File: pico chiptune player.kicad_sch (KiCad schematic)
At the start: 40 parts, among them J2 MicroSD, J3 Speaker_L, J4 Speaker_R, SW1 Play / Pause, SW2 Next, SW3 Previous, U1 YM2149F, U2 0.96"OLED_I2C, U3 PAM8403, U4 YM2149F

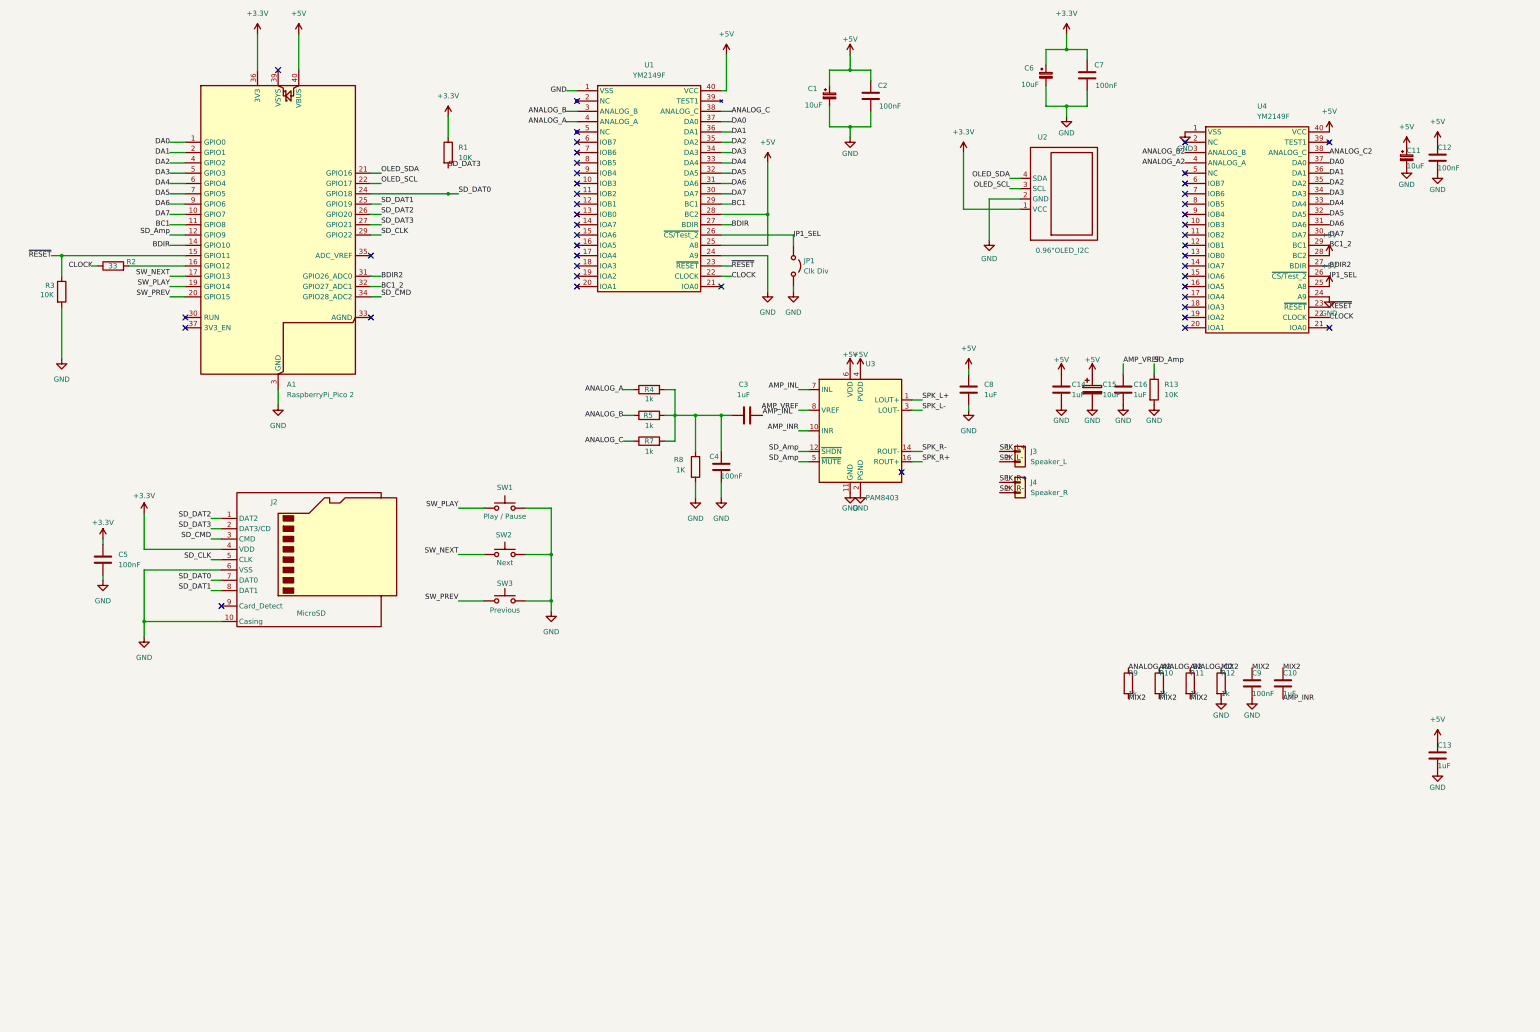
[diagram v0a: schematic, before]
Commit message: feat(hw): upgrade to Rev 0.7 with bare RP2354A, USB-C 3-stage sequencer, and 4-mode 74HCT4053D stereo/mono mixing matrix
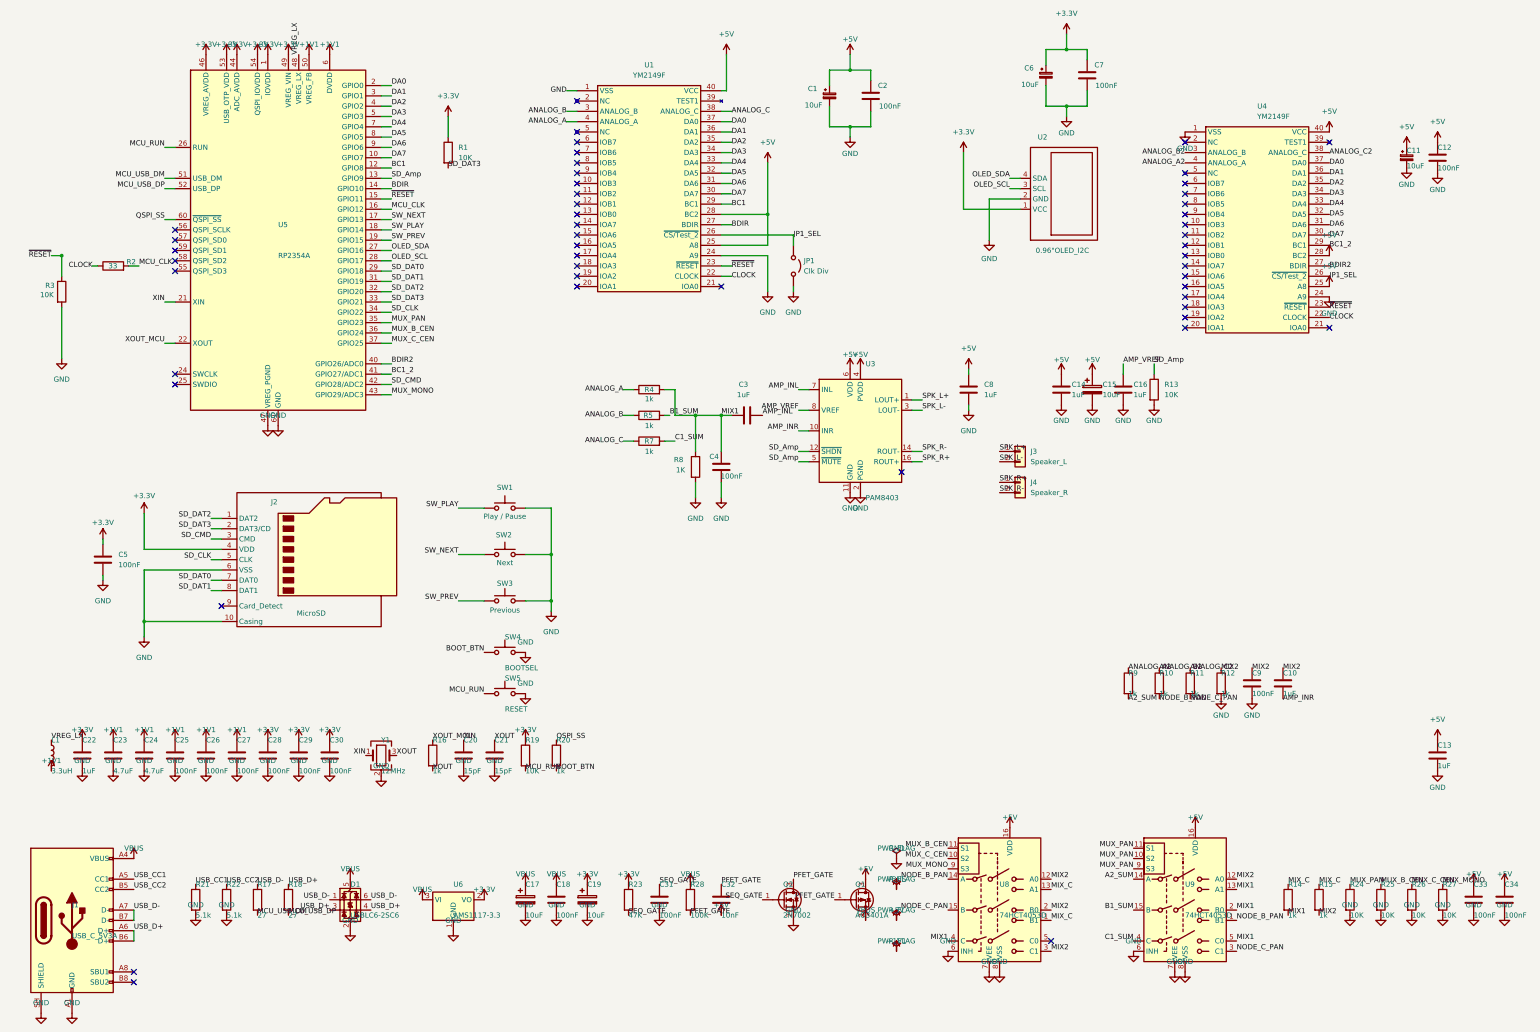
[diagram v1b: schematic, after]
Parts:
- removed A1: RaspberryPi_Pico 2, TMCu Module:RPi_Pico_SMD_TH, symbol MCU_Module_RaspberryPi_Pico:RaspberryPi_Pico
- added C17, C19: 10uF, Capacitor_SMD:CP_Elec_4x5.4, symbol Device:C_Polarized
- added C18, C25, C26, C27, C28, C29, C30, C31, C33, C34: 100nF, Capacitor_SMD:C_0805_2012Metric_Pad1.18x1.45mm_HandSolder, symbol Device:C
- added C20, C21: 15pF, Capacitor_SMD:C_0805_2012Metric_Pad1.18x1.45mm_HandSolder, symbol Device:C
- added C22: 1uF, Capacitor_SMD:C_0805_2012Metric_Pad1.18x1.45mm_HandSolder, symbol Device:C
- added C23, C24: 4.7uF, Capacitor_SMD:C_0805_2012Metric_Pad1.18x1.45mm_HandSolder, symbol Device:C
- added C32: 10nF, Capacitor_SMD:C_0805_2012Metric_Pad1.18x1.45mm_HandSolder, symbol Device:C
- added D1: USBLC6-2SC6, Package_TO_SOT_SMD:SOT-23-6, symbol Power_Protection:USBLC6-2SC6
- added J1: USB_C_5V3A, Connector_USB:USB_C_Receptacle_HRO_TYPE-C-31-M-12, symbol Connector:USB_C_Receptacle_USB2.0_16P
- added L1: 3.3uH, Inductor_SMD:L_1210_3225Metric, symbol Device:L
- added Q1: AO3401A, Package_TO_SOT_SMD:SOT-23, symbol Transistor_FET:AO3401A
- added Q2: 2N7002, Package_TO_SOT_SMD:SOT-23, symbol Transistor_FET:2N7002
- added R14, R15, R16, R20: 1k, Resistor_SMD:R_0805_2012Metric_Pad1.20x1.40mm_HandSolder, symbol Device:R
- added R17, R18: 27, Resistor_SMD:R_0805_2012Metric_Pad1.20x1.40mm_HandSolder, symbol Device:R
- added R19, R24, R25, R26, R27: 10K, Resistor_SMD:R_0805_2012Metric_Pad1.20x1.40mm_HandSolder, symbol Device:R
- added R21, R22: 5.1k, Resistor_SMD:R_0805_2012Metric_Pad1.20x1.40mm_HandSolder, symbol Device:R
- added R23: 47K, Resistor_SMD:R_0805_2012Metric_Pad1.20x1.40mm_HandSolder, symbol Device:R
- added R28: 100K, Resistor_SMD:R_0805_2012Metric_Pad1.20x1.40mm_HandSolder, symbol Device:R
- added SW4: BOOTSEL, Button_Switch_THT:SW_PUSH_6mm, symbol Switch:SW_Push
- added SW5: RESET, Button_Switch_THT:SW_PUSH_6mm, symbol Switch:SW_Push
- added U5: RP2354A, Package_DFN_QFN:QFN-60-1EP_7x7mm_P0.4mm_EP3.4x3.4mm, symbol MCU_RaspberryPi:RP2354A
- added U6: AMS1117-3.3, Package_TO_SOT_SMD:SOT-223-3_TabPin2, symbol Regulator_Linear:AMS1117-3.3
- added U8, U9: 74HCT4053D, Package_SO:SOIC-16_3.9x9.9mm_P1.27mm, symbol Analog_Switch:CD4053B
- added Y1: 12MHz, Crystal:Crystal_SMD_3225-4Pin_3.2x2.5mm, symbol Device:Crystal_GND24
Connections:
- net +3.3V: now also C19.1, C22.1, C28.1, C29.1, C30.1, R19.1, R23.1, U5.1 (IOVDD), U5.11 (IOVDD), U5.20 (IOVDD), U5.30 (IOVDD), U5.38 (IOVDD), U5.44 (ADC_AVDD), U5.45 (IOVDD), U5.46 (VREG_AVDD), U5.49 (VREG_VIN), U5.53 (USB_OTP_VDD), U5.54 (QSPI_IOVDD), U6.2 (VO)
- net +5V: now also C32.2, C33.1, C34.1, Q1.3 (D), U8.16 (VDD), U9.16 (VDD)
- net BC1: now also U5.12 (GPIO8)
- net BC1_2: now also U5.41 (GPIO27/ADC1)
- net BDIR: now also U5.14 (GPIO10)
- net BDIR2: now also U5.40 (GPIO26/ADC0)
- net DA0: now also U5.2 (GPIO0)
- net DA1: now also U5.3 (GPIO1)
- net DA2: now also U5.4 (GPIO2)
- net DA3: now also U5.5 (GPIO3)
- net DA4: now also U5.7 (GPIO4)
- net DA5: now also U5.8 (GPIO5)
- net DA6: now also U5.9 (GPIO6)
- net DA7: now also U5.10 (GPIO7)
- net GND: now also C17.2, C18.2, C19.2, C20.2, C21.2, C22.2, C23.2, C24.2, C25.2, C26.2, C27.2, C28.2, C29.2, C30.2, C31.2, C33.2, C34.2, D1.2 (GND), J1.A1 (GND), J1.A12 (GND), J1.B1 (GND), J1.B12 (GND), J1.SH (SHIELD), Q2.2 (S), R21.2, R22.2, R24.2, R25.2, R26.2, R27.2, SW4.2, SW5.2, U5.47 (VREG_PGND), U5.61 (GND), U6.1 (GND), U8.6 (INH), U8.7 (VEE), U8.8 (VSS), U9.6 (INH), U9.7 (VEE), U9.8 (VSS), Y1.2 (G), Y1.4 (G)
- net MIX2: now also R15.2, U8.12 (A0), U8.2 (B0), U8.3 (C1), U9.12 (A0); no longer R10.2, R11.2, R9.2
- net OLED_SCL: now also U5.28 (GPIO17)
- net OLED_SDA: now also U5.27 (GPIO16)
- net SD_Amp: now also U5.13 (GPIO9)
- net SD_CLK: now also U5.34 (GPIO22)
- net SD_CMD: now also U5.42 (GPIO28/ADC2)
- net SD_DAT0: now also U5.29 (GPIO18)
- net SD_DAT1: now also U5.31 (GPIO19)
- net SD_DAT2: now also U5.32 (GPIO20)
- net SD_DAT3: now also U5.33 (GPIO21)
- net SW_NEXT: now also U5.17 (GPIO13)
- net SW_PLAY: now also U5.18 (GPIO14)
- net SW_PREV: now also U5.19 (GPIO15)
- net ~{RESET}: now also U5.15 (GPIO11)
- net MIX1: now reaches C3.1, C4.1, R4.2, R8.1
- net MIX1: now also R14.2, U8.4 (C), U9.13 (A1), U9.2 (B0), U9.5 (C0); no longer R5.2, R7.2
- net MCU_CLK: now reaches R2.2
- net MCU_CLK: now also U5.16 (GPIO12)
- new net +1V1: C23.1, C24.1, C25.1, C26.1, C27.1, L1.2, U5.23 (DVDD), U5.39 (DVDD), U5.50 (VREG_FB), U5.6 (DVDD)
- new net A2_SUM: R9.2, U9.14 (A)
- new net B1_SUM: R5.2, U9.15 (B)
- new net BOOT_BTN: R20.2, SW4.1
- new net C1_SUM: R7.2, U9.4 (C)
- new net MCU_RUN: R19.2, SW5.1, U5.26 (RUN)
- new net MCU_USB_DM: R17.2, U5.51 (USB_DM)
- new net MCU_USB_DP: R18.2, U5.52 (USB_DP)
- new net MIX_C: R14.1, R15.1, U8.1 (B1), U8.13 (A1)
- new net MUX_B_CEN: R25.1, U5.36 (GPIO24), U8.11 (S1)
- new net MUX_C_CEN: R26.1, U5.37 (GPIO25), U8.10 (S2)
- new net MUX_MONO: R27.1, U5.43 (GPIO29/ADC3), U8.9 (S3)
- new net MUX_PAN: R24.1, U5.35 (GPIO23), U9.10 (S2), U9.11 (S1), U9.9 (S3)
- new net NODE_B_PAN: R10.2, U8.14 (A), U9.1 (B1)
- new net NODE_C_PAN: R11.2, U8.15 (B), U9.3 (C1)
- new net PFET_GATE: C32.1, Q1.1 (G), Q2.3 (D), R28.2
- new net QSPI_SS: R20.1, U5.60 (~{QSPI_SS})
- new net SEQ_GATE: C31.1, Q2.1 (G), R23.2
- new net USB_CC1: J1.A5 (CC1), R21.1
- new net USB_CC2: J1.B5 (CC2), R22.1
- new net USB_D+: D1.3 (I/O2), D1.4 (I/O2), J1.A6 (D+), J1.B6 (D+), R18.1
- new net USB_D-: D1.1 (I/O1), D1.6 (I/O1), J1.A7 (D-), J1.B7 (D-), R17.1
- new net VBUS: C17.1, C18.1, D1.5 (VBUS), J1.A4 (VBUS), J1.A9 (VBUS), J1.B4 (VBUS), J1.B9 (VBUS), Q1.2 (S), R28.1, U6.3 (VI)
- new net VREG_LX: L1.1, U5.48 (VREG_LX)
- new net XIN: C20.1, U5.21 (XIN), Y1.1
- new net XOUT: C21.1, R16.2, Y1.3
- new net XOUT_MCU: R16.1, U5.22 (XOUT)
- no-connect marks 44 -> 49

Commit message: Implement code changes to enhance functionality and improve performance
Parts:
- removed C17, C19: 10uF, Capacitor_SMD:CP_Elec_4x5.4, symbol Device:C_Polarized
- removed C18, C25, C26, C27, C28, C29, C30, C31, C33, C34: 100nF, Capacitor_SMD:C_0805_2012Metric_Pad1.18x1.45mm_HandSolder, symbol Device:C
- removed C20, C21: 15pF, Capacitor_SMD:C_0805_2012Metric_Pad1.18x1.45mm_HandSolder, symbol Device:C
- removed C22: 1uF, Capacitor_SMD:C_0805_2012Metric_Pad1.18x1.45mm_HandSolder, symbol Device:C
- removed C23, C24: 4.7uF, Capacitor_SMD:C_0805_2012Metric_Pad1.18x1.45mm_HandSolder, symbol Device:C
- removed C32: 10nF, Capacitor_SMD:C_0805_2012Metric_Pad1.18x1.45mm_HandSolder, symbol Device:C
- removed D1: USBLC6-2SC6, Package_TO_SOT_SMD:SOT-23-6, symbol Power_Protection:USBLC6-2SC6
- removed J1: USB_C_5V3A, Connector_USB:USB_C_Receptacle_HRO_TYPE-C-31-M-12, symbol Connector:USB_C_Receptacle_USB2.0_16P
- removed L1: 3.3uH, Inductor_SMD:L_1210_3225Metric, symbol Device:L
- removed Q1: AO3401A, Package_TO_SOT_SMD:SOT-23, symbol Transistor_FET:AO3401A
- removed Q2: 2N7002, Package_TO_SOT_SMD:SOT-23, symbol Transistor_FET:2N7002
- removed R14, R15, R16, R20: 1k, Resistor_SMD:R_0805_2012Metric_Pad1.20x1.40mm_HandSolder, symbol Device:R
- removed R17, R18: 27, Resistor_SMD:R_0805_2012Metric_Pad1.20x1.40mm_HandSolder, symbol Device:R
- removed R19, R24, R25, R26, R27: 10K, Resistor_SMD:R_0805_2012Metric_Pad1.20x1.40mm_HandSolder, symbol Device:R
- removed R21, R22: 5.1k, Resistor_SMD:R_0805_2012Metric_Pad1.20x1.40mm_HandSolder, symbol Device:R
- removed R23: 47K, Resistor_SMD:R_0805_2012Metric_Pad1.20x1.40mm_HandSolder, symbol Device:R
- removed R28: 100K, Resistor_SMD:R_0805_2012Metric_Pad1.20x1.40mm_HandSolder, symbol Device:R
- removed SW4: BOOTSEL, Button_Switch_THT:SW_PUSH_6mm, symbol Switch:SW_Push
- removed SW5: RESET, Button_Switch_THT:SW_PUSH_6mm, symbol Switch:SW_Push
- removed U5: RP2354A, Package_DFN_QFN:QFN-60-1EP_7x7mm_P0.4mm_EP3.4x3.4mm, symbol MCU_RaspberryPi:RP2354A
- removed U6: AMS1117-3.3, Package_TO_SOT_SMD:SOT-223-3_TabPin2, symbol Regulator_Linear:AMS1117-3.3
- removed U8, U9: 74HCT4053D, Package_SO:SOIC-16_3.9x9.9mm_P1.27mm, symbol Analog_Switch:CD4053B
- removed Y1: 12MHz, Crystal:Crystal_SMD_3225-4Pin_3.2x2.5mm, symbol Device:Crystal_GND24
- added A1: RaspberryPi_Pico 2, TMCu Module:RPi_Pico_SMD_TH, symbol MCU_Module_RaspberryPi_Pico:RaspberryPi_Pico
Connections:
- net A2_SUM is gone; now on net MIX2: R9.2
- net C1_SUM is gone; now on an unnamed net: R7.2
- net MIX1 is gone; now on an unnamed net: C3.1, C4.1, R4.2, R8.1
- net NODE_B_PAN is gone; now on net MIX2: R10.2
- net NODE_C_PAN is gone; now on net MIX2: R11.2
- net +3.3V: now also A1.36 (3V3)
- net +5V: now also A1.40 (VBUS)
- net BC1: now also A1.11 (GPIO8)
- net BC1_2: now also A1.32 (GPIO27_ADC1)
- net BDIR: now also A1.14 (GPIO10)
- net BDIR2: now also A1.31 (GPIO26_ADC0)
- net DA0: now also A1.1 (GPIO0)
- net DA1: now also A1.2 (GPIO1)
- net DA2: now also A1.4 (GPIO2)
- net DA3: now also A1.5 (GPIO3)
- net DA4: now also A1.6 (GPIO4)
- net DA5: now also A1.7 (GPIO5)
- net DA6: now also A1.9 (GPIO6)
- net DA7: now also A1.10 (GPIO7)
- net GND: now also A1.13 (GND), A1.18 (GND), A1.23 (GND), A1.28 (GND), A1.3 (GND), A1.38 (GND), A1.8 (GND)
- net OLED_SCL: now also A1.22 (GPIO17)
- net OLED_SDA: now also A1.21 (GPIO16)
- net SD_Amp: now also A1.12 (GPIO9)
- net SD_CLK: now also A1.29 (GPIO22)
- net SD_CMD: now also A1.34 (GPIO28_ADC2)
- net SD_DAT0: now also A1.24 (GPIO18)
- net SD_DAT1: now also A1.25 (GPIO19)
- net SD_DAT2: now also A1.26 (GPIO20)
- net SD_DAT3: now also A1.27 (GPIO21)
- net SW_NEXT: now also A1.17 (GPIO13)
- net SW_PLAY: now also A1.19 (GPIO14)
- net SW_PREV: now also A1.20 (GPIO15)
- net ~{RESET}: now also A1.15 (GPIO11)
- net B1_SUM: no longer names the net of R5.2
- net MCU_CLK: no longer names the net of R2.2
- net MCU_CLK: now also A1.16 (GPIO12)
- no-connect marks 49 -> 44
